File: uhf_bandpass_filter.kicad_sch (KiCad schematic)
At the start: 20 parts

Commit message: More filter work. Add project title to drawings.
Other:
- company: (none) -> Steves Custom Computers
- title: (none) -> PLUTO RF Card Front-End
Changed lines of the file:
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@@
 (kicad_sch (version 20230121) (generator eeschema)
   (paper "A4")
+  (title_block
+    (title "PLUTO RF Card Front-End")
+    (rev " 001")
+    (company "Steves Custom Computers")
+  )
   (junction (at 80.01 90.17) (diameter 0) (color 0 0 0 0)
   )

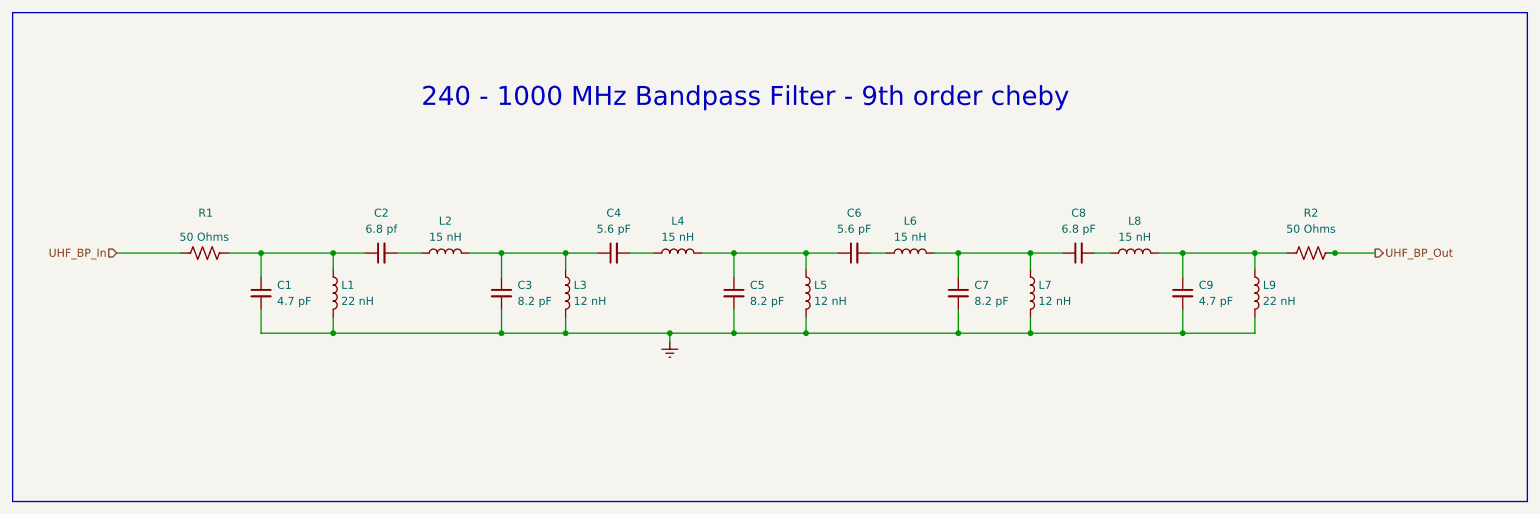
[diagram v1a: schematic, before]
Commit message: Major restructure. Add power/control busses.
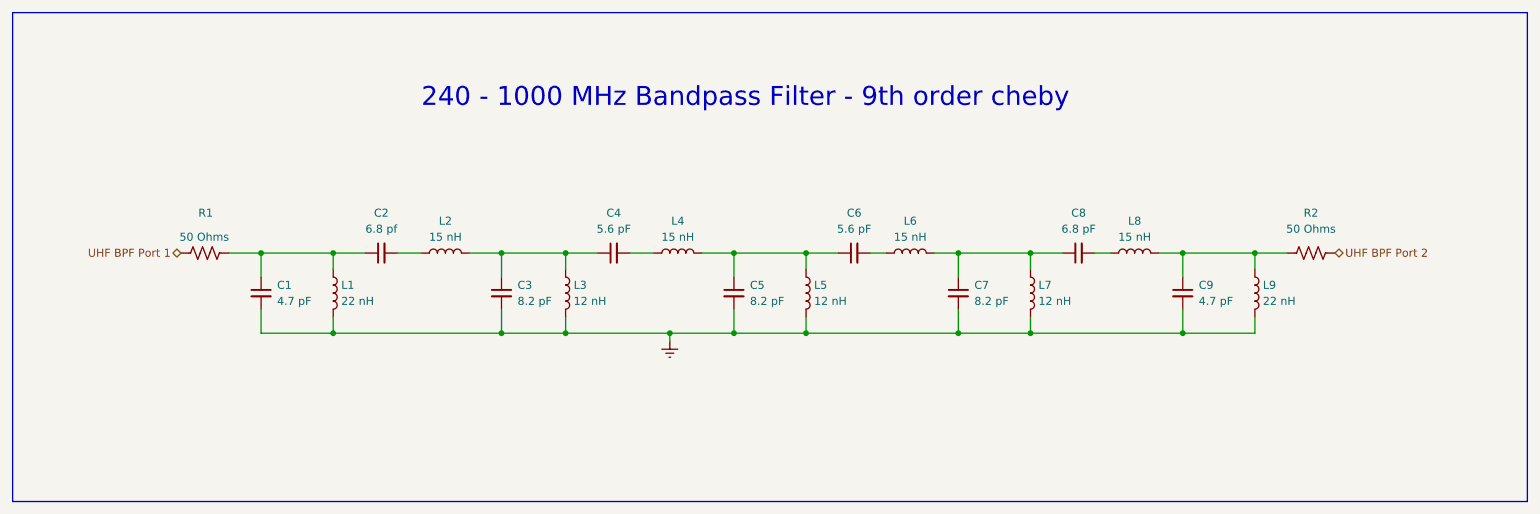
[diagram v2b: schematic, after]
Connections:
- net UHF_BP_In renamed UHF BPF Port 1
- net UHF_BP_Out renamed UHF BPF Port 2
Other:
- title: PLUTO RF Card Front-End -> PLUTO RF Front-End Card
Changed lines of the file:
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@@
   (paper "A4")
   (title_block
-    (title "PLUTO RF Card Front-End")
+    (title "PLUTO RF Front-End Card")
     (rev " 001")
     (company "Steves Custom Computers")
@@
   (junction (at 106.68 102.87) (diameter 0) (color 0 0 0 0)
   )
-  (junction (at 238.76 90.17) (diameter 0) (color 0 0 0 0)
-  )
   (junction (at 190.5 90.17) (diameter 0) (color 0 0 0 0)
   )
@@
     (stroke (width 0) (type default))
   )
-  (wire (pts (xy 237.49 90.17) (xy 238.76 90.17))
-    (stroke (width 0) (type default))
-  )
   (wire (pts (xy 68.58 102.87) (xy 80.01 102.87))
     (stroke (width 0) (type default))
@@
     (stroke (width 0) (type default))
   )
-  (wire (pts (xy 238.76 90.17) (xy 245.11 90.17))
-    (stroke (width 0) (type default))
-  )
   (wire (pts (xy 138.43 90.17) (xy 143.51 90.17))
     (stroke (width 0) (type default))
@@
   )
   (wire (pts (xy 226.06 90.17) (xy 226.06 92.71))
-    (stroke (width 0) (type default))
-  )
-  (wire (pts (xy 45.72 90.17) (xy 55.88 90.17))
     (stroke (width 0) (type default))
   )
@@
     (effects (font (size 3 3)) (justify left bottom))
   )
-  (hierarchical_label "UHF_BP_Out" (shape output) (at 245.11 90.17 0) (fields_autoplaced)
+  (hierarchical_label "UHF BPF Port 1" (shape bidirectional) (at 55.88 90.17 180) (fields_autoplaced)
+    (effects (font (size 1.27 1.27)) (justify right))
+  )
+  (hierarchical_label "UHF BPF Port 2" (shape bidirectional) (at 238.76 90.17 0) (fields_autoplaced)
     (effects (font (size 1.27 1.27)) (justify left))
   )
-  (hierarchical_label "UHF_BP_In" (shape input) (at 45.72 90.17 180) (fields_autoplaced)
-    (effects (font (size 1.27 1.27)) (justify right))
-  )
   (symbol (lib_id "Device:L") (at 116.84 96.52 0) (unit 1)
